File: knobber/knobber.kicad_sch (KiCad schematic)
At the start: 1 part, among them J101 BLDC

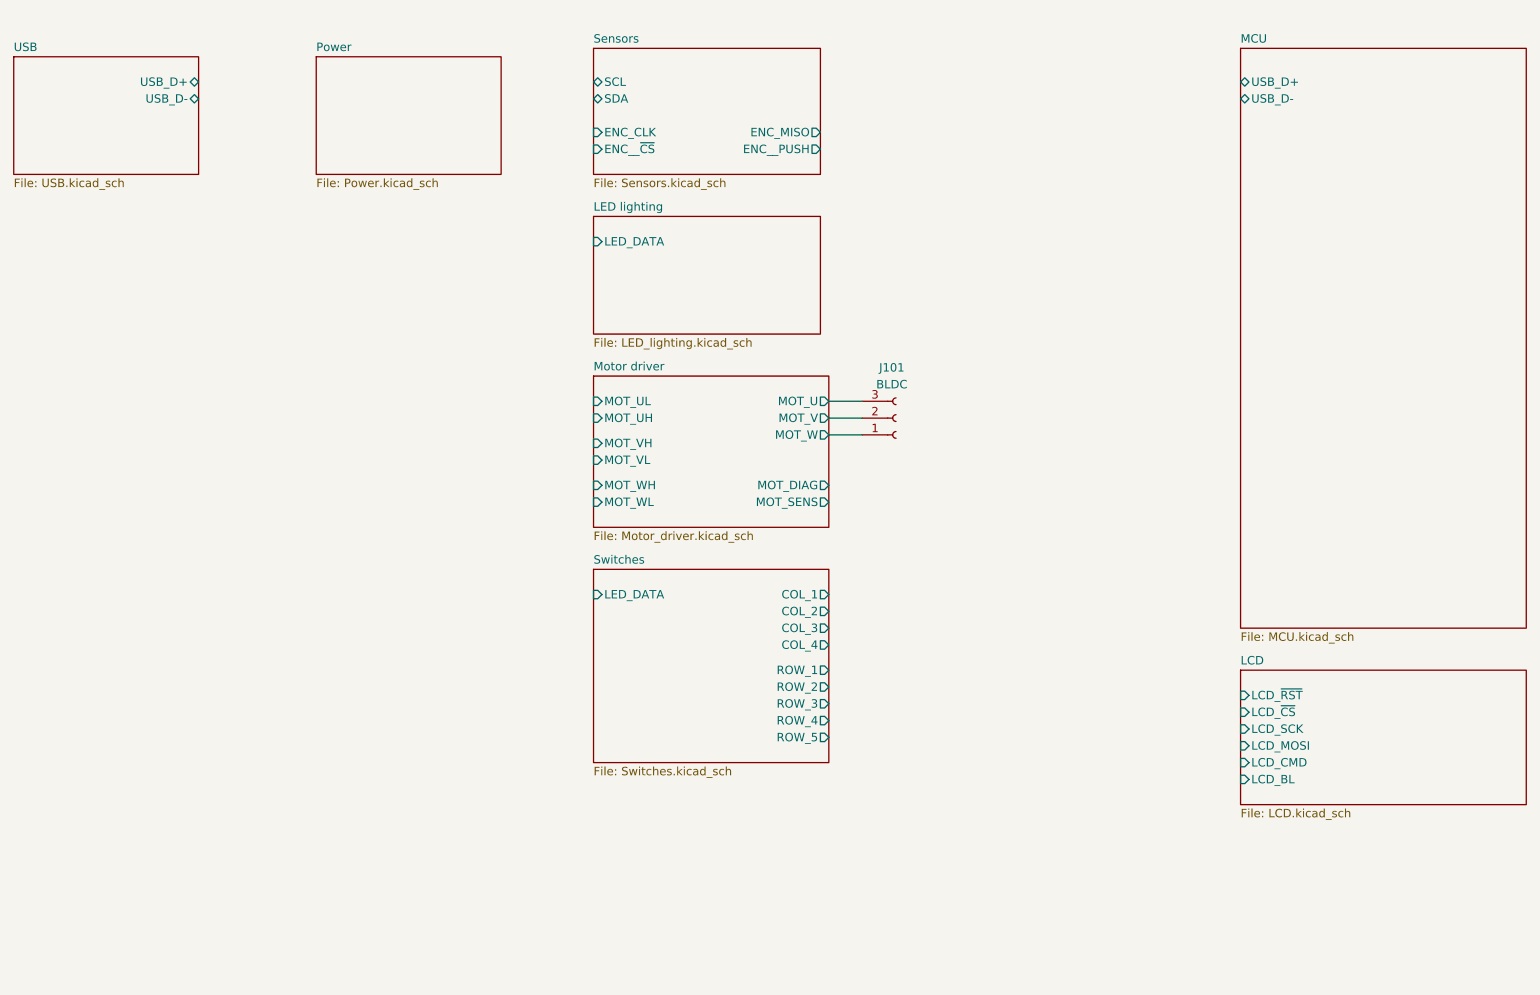
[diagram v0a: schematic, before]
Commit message: Updated schematic and PCB
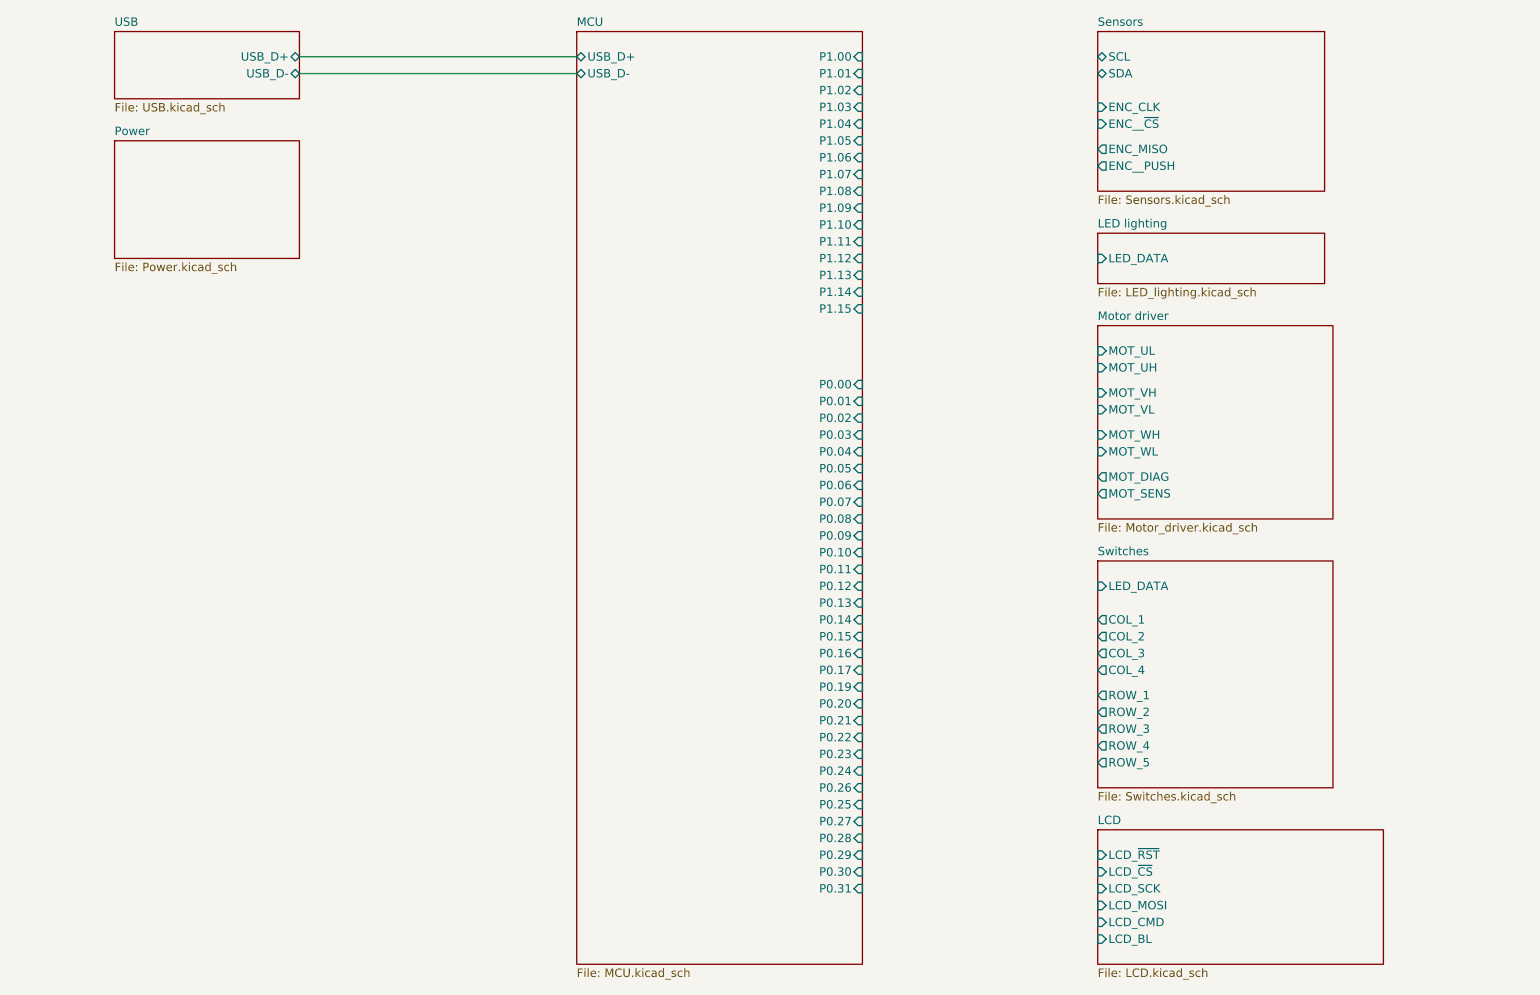
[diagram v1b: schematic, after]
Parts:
- removed J101: BLDC, Connector_Molex:Molex_SPOX_5267-03A_1x03_P2.50mm_Vertical, symbol Connector:Conn_01x03_Socket
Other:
- sheet MCU ports: added P0.00, P0.01, P0.02, P0.03, P0.04, P0.05, P0.06, P0.07, P0.08, P0.09, P0.10, P0.11, P0.12, P0.13, P0.14, P0.15, P0.16, P0.17, P0.19, P0.20, P0.21, P0.22, P0.23, P0.24, P0.25, P0.26, P0.27, P0.28, P0.29, P0.30, P0.31, P1.00, P1.01, P1.02, P1.03, P1.04, P1.05, P1.06, P1.07, P1.08, P1.09, P1.10, P1.11, P1.12, P1.13, P1.14, P1.15; removed none
- sheet Motor driver ports: added none; removed MOT_U, MOT_V, MOT_W
